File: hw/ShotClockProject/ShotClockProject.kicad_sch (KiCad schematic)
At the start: 5 parts, among them SW1 PS-5824SVB-6PL

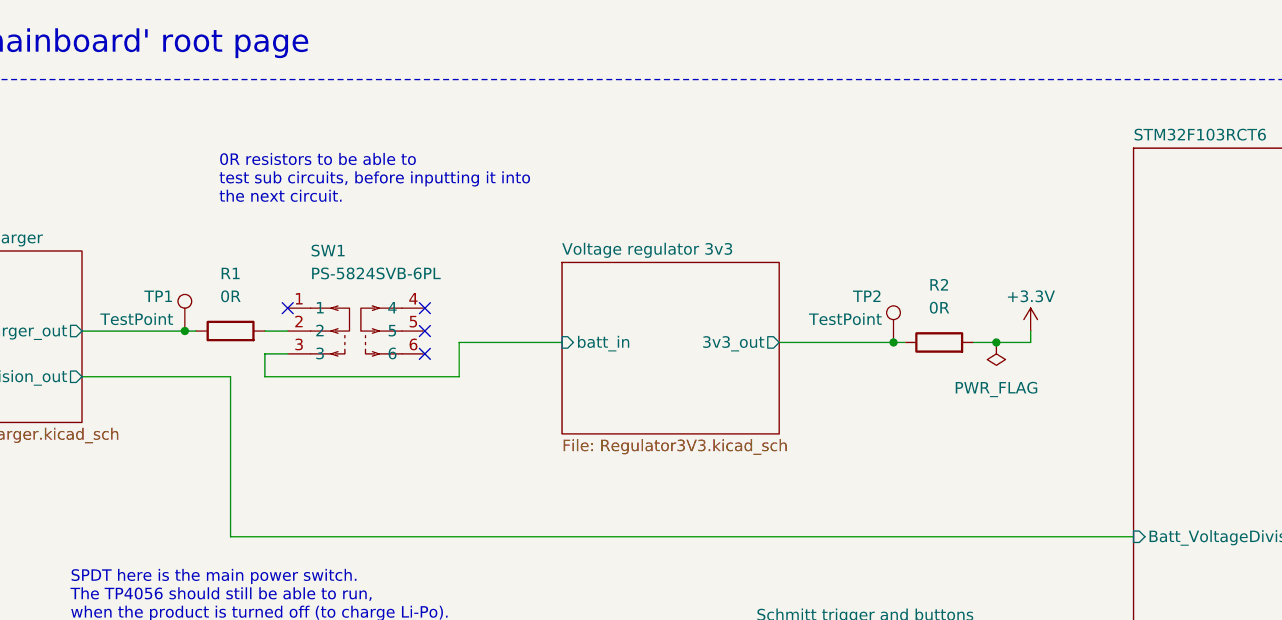
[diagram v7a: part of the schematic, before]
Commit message: Started on second PCB, and added 5V regulator
5V regulator added to main pcb for the segment displays, using same TPS63000 chip, but with a different selector resistor to choose for 5V

Added second project to contain the display PCBA design.

Calculated the current usage of the displays with different current limiting resistors on the LEDs.

Calculated the  current limit resistors for transistors behind LEDs
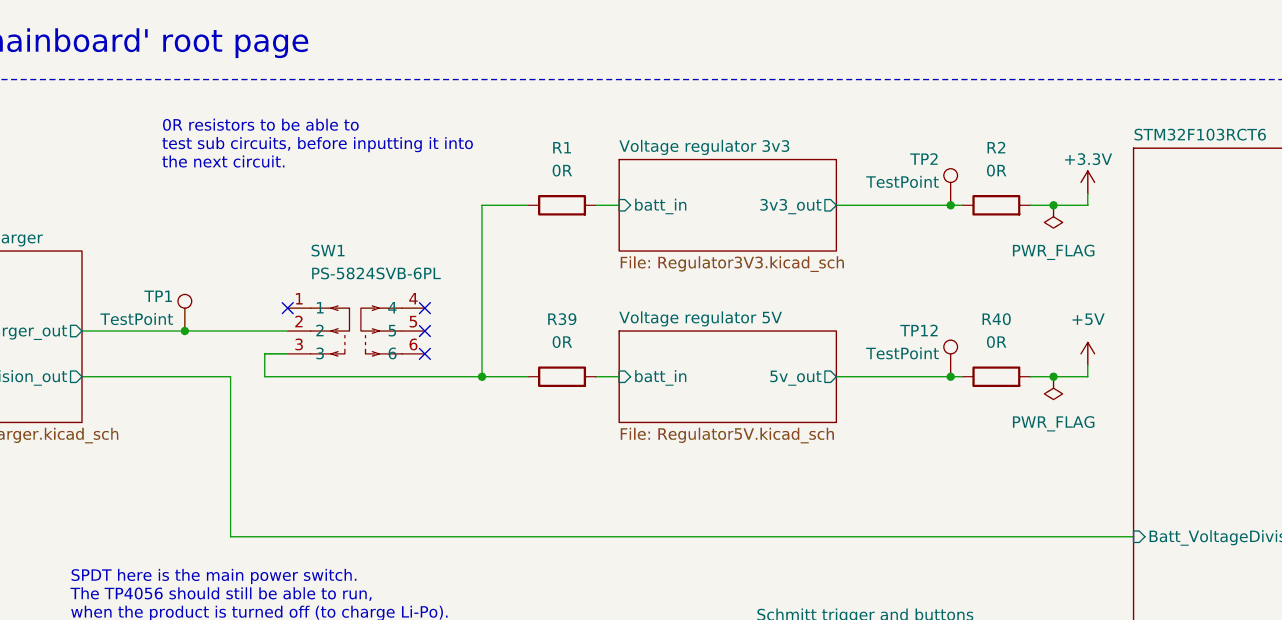
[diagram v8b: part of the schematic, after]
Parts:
- added R39, R40: 0R, Resistor_SMD:R_0402_1005Metric, symbol Device:R
- added TP12: TestPoint, TestPoint:TestPoint_Pad_D2.5mm, symbol Connector:TestPoint
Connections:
- net Li-Po Battery and charger/charger_out: now also SW1.2; no longer R1.1
- net Voltage regulator 3v3/batt_in: now also R1.2; no longer SW1.3
- new net: R1.1, R39.1, SW1.3
- new net +5V: R40.2
- new net Voltage regulator 5V/5v_out: R40.1, TP12.1
- new net Voltage regulator 5V/batt_in: R39.2
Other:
- added sheet Voltage regulator 5V (Regulator5V.kicad_sch)
- moved on the sheet: R2, TP2
